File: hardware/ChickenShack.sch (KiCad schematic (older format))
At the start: 44 parts, among them P1 BATTERY, P2 D_SENSE2, P3 SCOPE, P4 DEBUG, P5 D_MOTOR, P6 LIGHT, P7 D_SENSOR, P8 D_SWITCH, Q1 MOSFET_N, Q2 MOSFET_P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

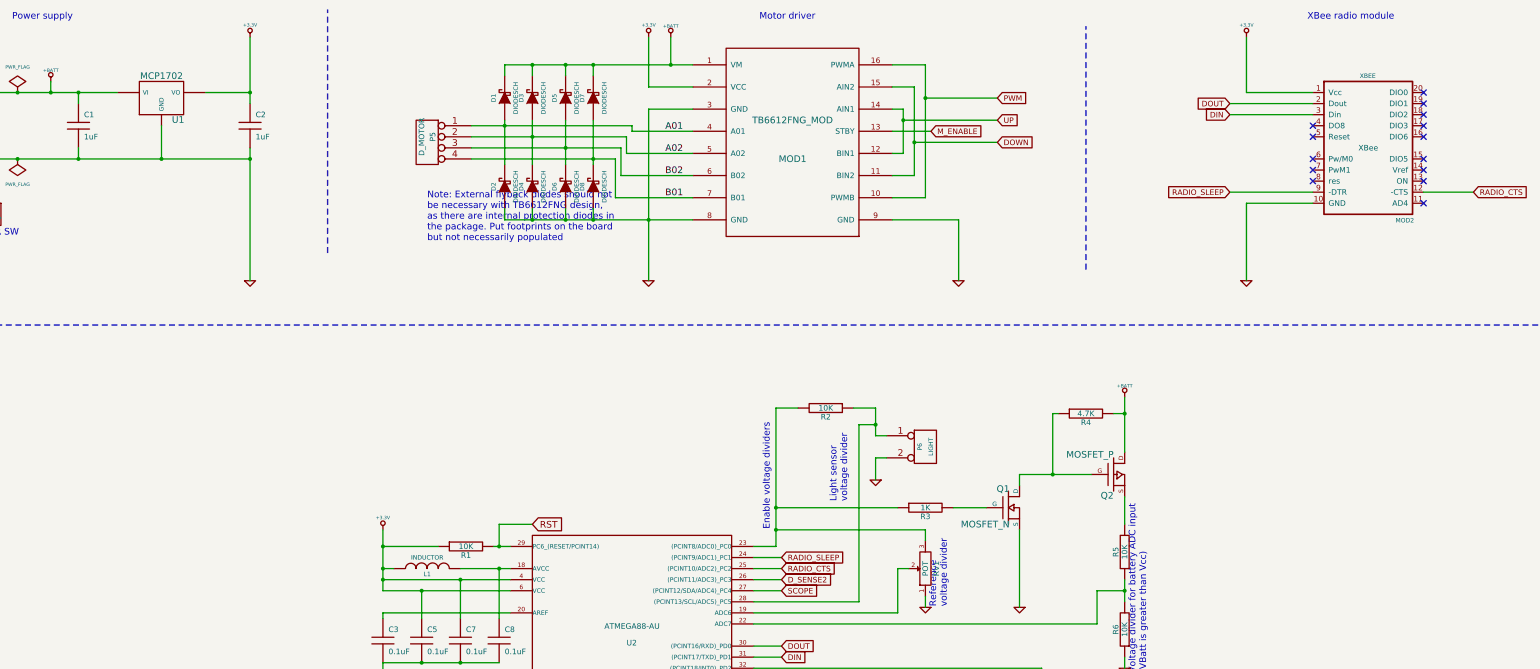
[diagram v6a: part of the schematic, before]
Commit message: Add test points, start routing PCB
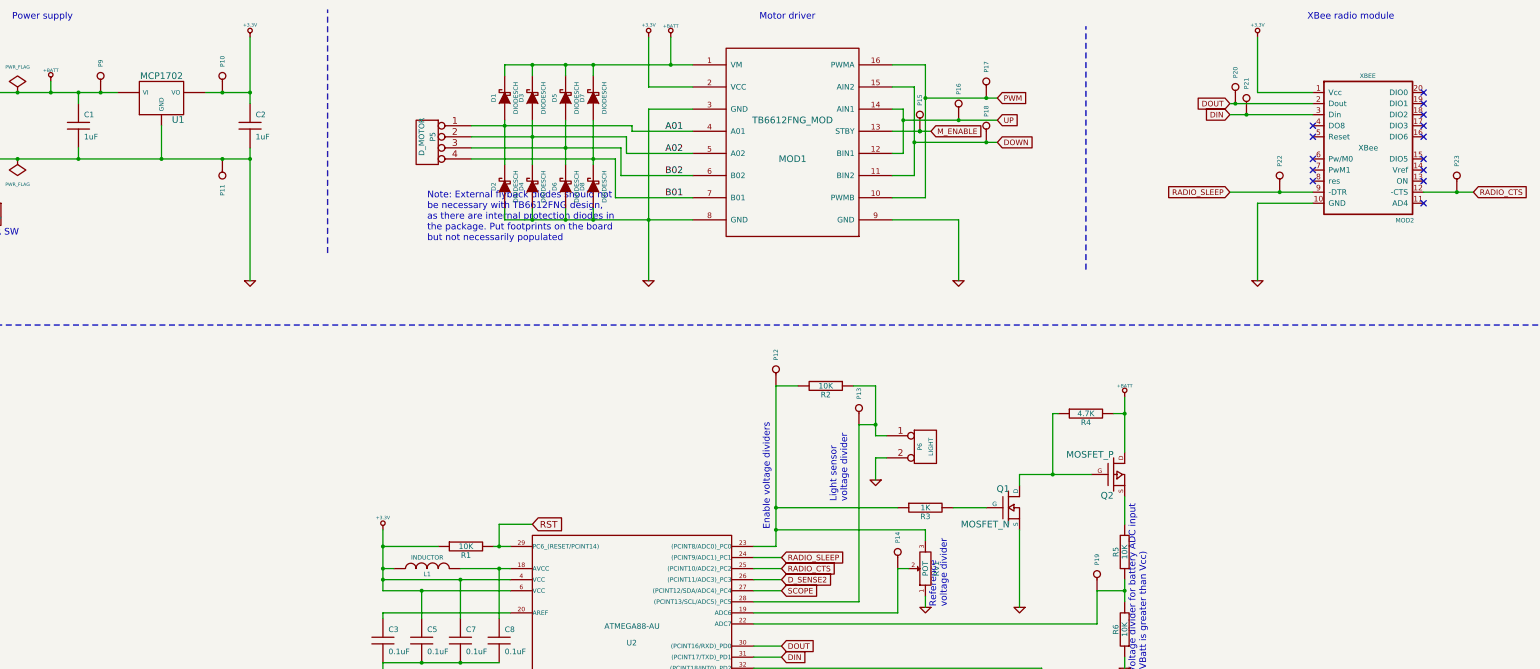
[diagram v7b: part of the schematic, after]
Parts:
- added P10, P11, P12, P13, P14, P15, P16, P17, P18, P19, P20, P21, P22, P23, P9: CONN_1, symbol CONN_1
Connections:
- net +3.3V: now also P10.1
- net +BATT: now also P9.1
- net DIN: now also P21.1
- net DOUT: now also P20.1
- net DOWN: now also P18.1
- net GND: now also P11.1
- net M_ENABLE: now also P15.1
- net PWM: now also P17.1
- net RADIO_CTS: now also P23.1
- net RADIO_SLEEP: now also P22.1
- net UP: now also P16.1
- net at RV1.2, U2.19 (ADC6): now also P14.1
- net at R5.1, R6.2, U2.22 (ADC7): now also P19.1
- net at R2.2, R3.1, RV1.3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: now also P12.1
- net at P6.1 (P1), R2.1, U2.28 ((PCINT13/SCL/ADC5)_PC5): now also P13.1
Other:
- moved on the sheet: R2
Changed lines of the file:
@@
-EESchema Schematic File Version 2  date Fri 04 Jan 2013 23:43:48 GMT
+EESchema Schematic File Version 2  date Sat 05 Jan 2013 12:54:03 GMT
 LIBS:dresco
 LIBS:ChickenShack-cache
@@
 Sheet 1 1
 Title ""
-Date "4 jan 2013"
+Date "5 jan 2013"
 Rev "2.00"
 Comp ""
@@
 Comment4 ""
 $EndDescr
+Connection ~ 14700 2400
+Connection ~ 13100 2400
+Connection ~ 12800 1700
+Connection ~ 12700 1600
+Connection ~ 9850 1850
+Connection ~ 10200 1750
+Connection ~ 10450 1950
+Connection ~ 10450 1550
+Connection ~ 9850 1850
+Connection ~ 2450 1500
+Connection ~ 3550 1500
+Connection ~ 3550 2100
+$Comp
+L CONN_1 P11
+U 1 1 50E82200
+P 3550 2250
+F 0 "P11" H 3630 2250 40  0000 L CNN
+F 1 "CONN_1" H 3550 2305 30  0001 C CNN
+	1    3550 2250
+	0    -1   1    0
+$EndComp
+$Comp
+L CONN_1 P10
+U 1 1 50E821F9
+P 3550 1350
+F 0 "P10" H 3630 1350 40  0000 L CNN
+F 1 "CONN_1" H 3550 1405 30  0001 C CNN
+	1    3550 1350
+	0    -1   -1   0
+$EndComp
+$Comp
+L CONN_1 P9
+U 1 1 50E821F3
+P 2450 1350
+F 0 "P9" H 2530 1350 40  0000 L CNN
+F 1 "CONN_1" H 2450 1405 30  0001 C CNN
+	1    2450 1350
+	0    -1   -1   0
+$EndComp
+$Comp
+L CONN_1 P15
+U 1 1 50E821DE
+P 9850 1700
+F 0 "P15" H 9930 1700 40  0000 L CNN
+F 1 "CONN_1" H 9850 1755 30  0001 C CNN
+	1    9850 1700
+	0    -1   -1   0
+$EndComp
+$Comp
+L CONN_1 P18
+U 1 1 50E821DB
+P 10450 1800
+F 0 "P18" H 10530 1800 40  0000 L CNN
+F 1 "CONN_1" H 10450 1855 30  0001 C CNN
+	1    10450 1800
+	0    -1   -1   0
+$EndComp
+$Comp
+L CONN_1 P16
+U 1 1 50E821D7
+P 10200 1600
+F 0 "P16" H 10280 1600 40  0000 L CNN
+F 1 "CONN_1" H 10200 1655 30  0001 C CNN
+	1    10200 1600
+	0    -1   -1   0
+$EndComp
+$Comp
+L CONN_1 P17
+U 1 1 50E821D2
+P 10450 1400
+F 0 "P17" H 10530 1400 40  0000 L CNN
+F 1 "CONN_1" H 10450 1455 30  0001 C CNN
+	1    10450 1400
+	0    -1   -1   0
+$EndComp
+$Comp
+L CONN_1 P21
+U 1 1 50E821B3
+P 12800 1550
+F 0 "P21" H 12880 1550 40  0000 L CNN
+F 1 "CONN_1" H 12800 1605 30  0001 C CNN
+	1    12800 1550
+	0    -1   -1   0
+$EndComp
+$Comp
+L CONN_1 P20
+U 1 1 50E821AF
+P 12700 1450
+F 0 "P20" H 12780 1450 40  0000 L CNN
+F 1 "CONN_1" H 12700 1505 30  0001 C CNN
+	1    12700 1450
+	0    -1   -1   0
+$EndComp
+$Comp
+L CONN_1 P23
+U 1 1 50E8219B
+P 14700 2250
+F 0 "P23" H 14780 2250 40  0000 L CNN
+F 1 "CONN_1" H 14700 2305 30  0001 C CNN
+	1    14700 2250
+	0    -1   -1   0
+$EndComp
+$Comp
+L CONN_1 P12
+U 1 1 50E82156
+P 8550 4000
+F 0 "P12" H 8630 4000 40  0000 L CNN
+F 1 "CONN_1" H 8550 4055 30  0001 C CNN
+	1    8550 4000
+	0    -1   -1   0
+$EndComp
+$Comp
+L CONN_1 P22
+U 1 1 50E82111
+P 13100 2250
+F 0 "P22" H 13180 2250 40  0000 L CNN
+F 1 "CONN_1" H 13100 2305 30  0001 C CNN
+	1    13100 2250
+	0    -1   -1   0
+$EndComp
+$Comp
+L CONN_1 P13
+U 1 1 50E820DE
+P 9300 4350
+F 0 "P13" H 9380 4350 40  0000 L CNN
+F 1 "CONN_1" H 9300 4405 30  0001 C CNN
+	1    9300 4350
+	0    -1   -1   0
+$EndComp
+$Comp
+L CONN_1 P14
+U 1 1 50E820D8
+P 9650 5650
+F 0 "P14" H 9730 5650 40  0000 L CNN
+F 1 "CONN_1" H 9650 5705 30  0001 C CNN
+	1    9650 5650
+	0    -1   -1   0
+$EndComp
+$Comp
+L CONN_1 P19
+U 1 1 50E820D0
+P 11450 5850
+F 0 "P19" H 11530 5850 40  0000 L CNN
+F 1 "CONN_1" H 11450 5905 30  0001 C CNN
+	1    11450 5850
+	0    -1   -1   0
+$EndComp
 Text Notes 2300 10100 0    60   ~ 0
 DOOR TENSION\nMICRO SWITCH
@@
 	3800 2000 3800 3200
 Wire Wire Line
-	2250 2000 2250 2100
+	2250 2100 2250 2000
 Wire Wire Line
 	1200 2200 1200 1500
@@
 	900  3600 15650 3600
 Wire Wire Line
-	8750 4350 8550 4350
-Wire Wire Line
-	8550 4350 8550 5600
-Wire Wire Line
-	9450 4600 9450 4350
+	8750 4150 8550 4150
+Wire Wire Line
+	8550 4150 8550 5600
+Wire Wire Line
+	9450 4600 9450 4150
 Wire Wire Line
 	10750 5050 10750 4950
@@
 	8600 6500 8350 6500
 Wire Wire Line
-	3800 1500 3400 1500
+	3400 1500 3800 1500
 Connection ~ 3000 2100
 Wire Wire Line
@@
 	13400 1600 12650 1600
 Wire Wire Line
-	12800 1000 12800 1500
-Wire Wire Line
-	12800 1500 13400 1500
+	12900 1000 12900 1500
+Wire Wire Line
+	12900 1500 13400 1500
 Connection ~ 6900 2100
 Connection ~ 6650 2000
@@
 	6900 2150 6900 1750
 Wire Wire Line
-	13400 2500 12800 2500
-Wire Wire Line
-	12800 2500 12800 3200
+	13400 2500 12900 2500
+Wire Wire Line
+	12900 2500 12900 3200
 Wire Wire Line
 	13400 1700 12650 1700
@@
 	9450 4800 9450 5000
 Wire Wire Line
-	9450 4350 9250 4350
+	9450 4150 9250 4150
 Wire Wire Line
 	8600 7200 8350 7200
@@
 L R R2
 U 1 1 50E1A55D
-P 9000 4350
-F 0 "R2" V 9080 4350 50  0000 C CNN
-F 1 "10K" V 9000 4350 50  0000 C CNN
-	1    9000 4350
+P 9000 4150
+F 0 "R2" V 9080 4150 50  0000 C CNN
+F 1 "10K" V 9000 4150 50  0000 C CNN
+	1    9000 4150
 	0    1    1    0
 $EndComp
@@
 L GND #PWR016
 U 1 1 4C4AB2CA
-P 12800 3200
-F 0 "#PWR016" H 12800 3200 30  0001 C CNN
-F 1 "GND" H 12800 3130 30  0001 C CNN
-	1    12800 3200
+P 12900 3200
+F 0 "#PWR016" H 12900 3200 30  0001 C CNN
+F 1 "GND" H 12900 3130 30  0001 C CNN
+	1    12900 3200
 	1    0    0    -1
 $EndComp
@@
 L +3.3V #PWR017
 U 1 1 4C4AB2C5
-P 12800 1000
-F 0 "#PWR017" H 12800 960 30  0001 C CNN
-F 1 "+3.3V" H 12800 1110 30  0000 C CNN
-	1    12800 1000
-	1    0    0    -1
-$EndComp
+P 12900 1000
+F 0 "#PWR017" H 12900 960 30  0001 C CNN
+F 1 "+3.3V" H 12900 1110 30  0000 C CNN
+	1    12900 1000
+	1    0    0    -1
+$EndComp
